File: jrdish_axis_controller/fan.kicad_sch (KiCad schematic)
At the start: 5 parts, among them CN5 KF2EDGR-2.54-2P, Q2 AO3400A

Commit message: PCB layout in progress
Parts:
- added C44: 10nF, PCM_JLCPCB:C_0402, symbol PCM_JLCPCB-Capacitors:0402,10nF
- added C45: 100nF, PCM_JLCPCB:C_0402, symbol PCM_JLCPCB-Capacitors:0402,100nF,(2)
- renumbered CN5 to CN6, R25 to R26, R26 to R27
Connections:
- net 12V: now also C44.1, C45.1
- net GND: now also C44.2, C45.2
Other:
- note added: "Place caps close to connector"
- company: (none) -> JRSeti
- moved on the sheet: CN6

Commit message: Continuing layout
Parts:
- renumbered C44 to C55, C45 to C56, CN6 to CN12, R26 to R27, R27 to R28
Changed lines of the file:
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@@
 		(in_pos_files yes)
 		(dnp no)
-		(property "Reference" "CN6"
+		(property "Reference" "CN12"
 			(at 117.348 76.454 0)
 			(show_name no)
@@
 			(project "jrdish_axis_controller"
 				(path "/10d7c3e5-be4d-4306-a59e-500b86bd141f/6fa2ea64-bed8-4819-9f4d-803f6e804a23"
-					(reference "CN6")
+					(reference "CN12")
 					(unit 1)
 				)
@@
 		(in_pos_files yes)
 		(dnp no)
-		(property "Reference" "#PWR040"
+		(property "Reference" "#PWR046"
 			(at 128.27 90.17 0)
 			(hide yes)
@@
 			(project "jrdish_axis_controller"
 				(path "/10d7c3e5-be4d-4306-a59e-500b86bd141f/6fa2ea64-bed8-4819-9f4d-803f6e804a23"
-					(reference "#PWR040")
+					(reference "#PWR046")
 					(unit 1)
 				)
@@
 		(dnp no)
 		(fields_autoplaced yes)
-		(property "Reference" "R26"
+		(property "Reference" "R27"
 			(at 133.35 90.17 90)
 			(show_name no)
@@
 			(project "jrdish_axis_controller"
 				(path "/10d7c3e5-be4d-4306-a59e-500b86bd141f/6fa2ea64-bed8-4819-9f4d-803f6e804a23"
-					(reference "R26")
+					(reference "R27")
 					(unit 1)
 				)
@@
 		(dnp no)
 		(fields_autoplaced yes)
-		(property "Reference" "R27"
+		(property "Reference" "R28"
 			(at 130.81 99.0599 0)
 			(show_name no)
@@
 			(project "jrdish_axis_controller"
 				(path "/10d7c3e5-be4d-4306-a59e-500b86bd141f/6fa2ea64-bed8-4819-9f4d-803f6e804a23"
-					(reference "R27")
+					(reference "R28")
 					(unit 1)
 				)
@@
 		(in_pos_files yes)
 		(dnp no)
-		(property "Reference" "C44"
+		(property "Reference" "C55"
 			(at 126.238 76.4539 0)
 			(show_name no)
@@
 			(project "jrdish_axis_controller"
 				(path "/10d7c3e5-be4d-4306-a59e-500b86bd141f/6fa2ea64-bed8-4819-9f4d-803f6e804a23"
-					(reference "C44")
+					(reference "C55")
 					(unit 1)
 				)
@@
 		(in_pos_files yes)
 		(dnp no)
-		(property "Reference" "#PWR041"
+		(property "Reference" "#PWR047"
 			(at 137.16 111.76 0)
 			(hide yes)
@@
 			(project "jrdish_axis_controller"
 				(path "/10d7c3e5-be4d-4306-a59e-500b86bd141f/6fa2ea64-bed8-4819-9f4d-803f6e804a23"
-					(reference "#PWR041")
+					(reference "#PWR047")
 					(unit 1)
 				)
@@
 		(in_pos_files yes)
 		(dnp no)
-		(property "Reference" "C45"
+		(property "Reference" "C56"
 			(at 133.604 76.1999 0)
 			(show_name no)
@@
 			(project "jrdish_axis_controller"
 				(path "/10d7c3e5-be4d-4306-a59e-500b86bd141f/6fa2ea64-bed8-4819-9f4d-803f6e804a23"
-					(reference "C45")
+					(reference "C56")
 					(unit 1)
 				)

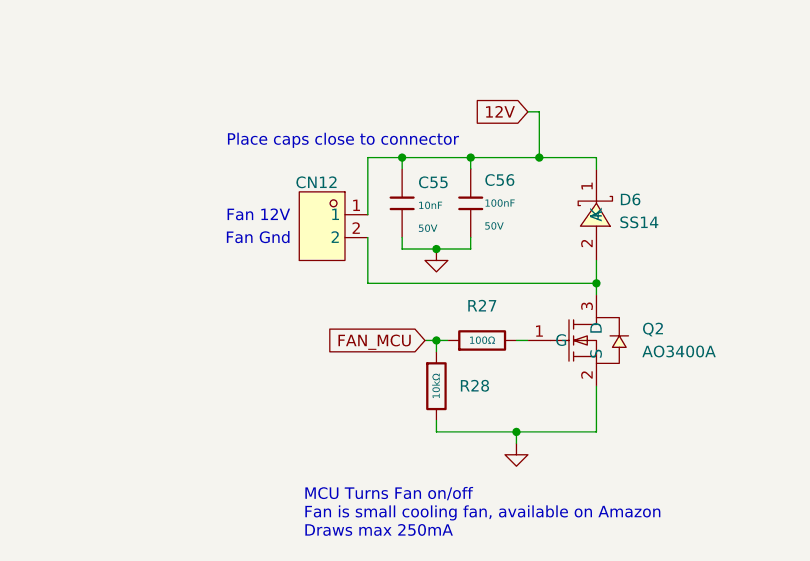
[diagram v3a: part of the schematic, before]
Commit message: RS485 isolated areas in place
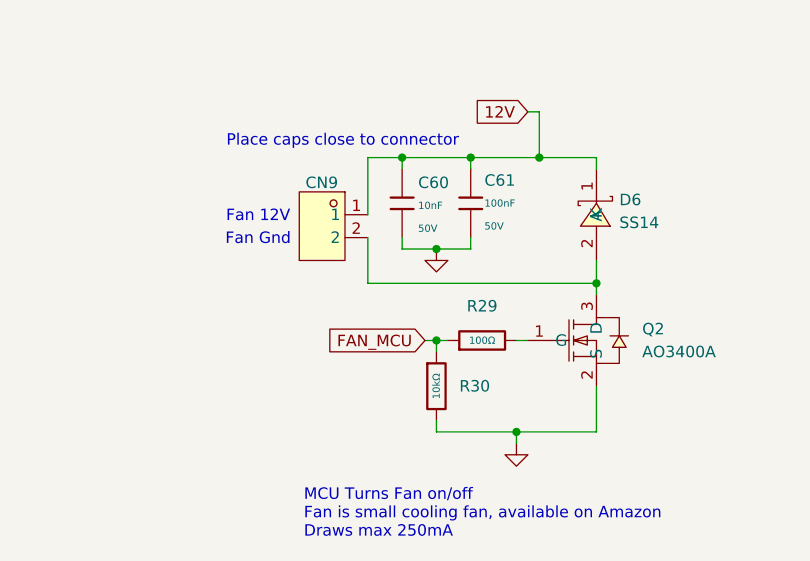
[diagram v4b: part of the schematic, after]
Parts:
- renumbered C55 to C60, C56 to C61, CN12 to CN9, R27 to R29, R28 to R30
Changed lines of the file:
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@@
 		(in_pos_files yes)
 		(dnp no)
-		(property "Reference" "CN12"
+		(property "Reference" "CN9"
 			(at 117.348 76.454 0)
 			(show_name no)
@@
 			(project "jrdish_axis_controller"
 				(path "/10d7c3e5-be4d-4306-a59e-500b86bd141f/6fa2ea64-bed8-4819-9f4d-803f6e804a23"
-					(reference "CN12")
+					(reference "CN9")
 					(unit 1)
 				)
@@
 		(dnp no)
 		(fields_autoplaced yes)
-		(property "Reference" "R27"
+		(property "Reference" "R29"
 			(at 133.35 90.17 90)
 			(show_name no)
@@
 			(project "jrdish_axis_controller"
 				(path "/10d7c3e5-be4d-4306-a59e-500b86bd141f/6fa2ea64-bed8-4819-9f4d-803f6e804a23"
-					(reference "R27")
+					(reference "R29")
 					(unit 1)
 				)
@@
 		(dnp no)
 		(fields_autoplaced yes)
-		(property "Reference" "R28"
+		(property "Reference" "R30"
 			(at 130.81 99.0599 0)
 			(show_name no)
@@
 			(project "jrdish_axis_controller"
 				(path "/10d7c3e5-be4d-4306-a59e-500b86bd141f/6fa2ea64-bed8-4819-9f4d-803f6e804a23"
-					(reference "R28")
+					(reference "R30")
 					(unit 1)
 				)
@@
 		(in_pos_files yes)
 		(dnp no)
-		(property "Reference" "C55"
+		(property "Reference" "C60"
 			(at 126.238 76.4539 0)
 			(show_name no)
@@
 			(project "jrdish_axis_controller"
 				(path "/10d7c3e5-be4d-4306-a59e-500b86bd141f/6fa2ea64-bed8-4819-9f4d-803f6e804a23"
-					(reference "C55")
+					(reference "C60")
 					(unit 1)
 				)
@@
 		(in_pos_files yes)
 		(dnp no)
-		(property "Reference" "C56"
+		(property "Reference" "C61"
 			(at 133.604 76.1999 0)
 			(show_name no)
@@
 			(project "jrdish_axis_controller"
 				(path "/10d7c3e5-be4d-4306-a59e-500b86bd141f/6fa2ea64-bed8-4819-9f4d-803f6e804a23"
-					(reference "C56")
+					(reference "C61")
 					(unit 1)
 				)

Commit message: Making refinements
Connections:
- net GND: no longer names the net of Q2.2 (S), R30.2
- net GND: no longer C60.2, C61.2
- new net: C60.2, C61.2
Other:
- title: (none) -> Fan
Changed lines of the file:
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@@
 	(paper "A4")
 	(title_block
-		(date "2026-04-12")
+		(title "Fan")
+		(date "2026-04-30")
 		(rev "1.0")
 		(company "JRSeti")

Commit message: Limit switches with mosfets
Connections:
- net GND: now reaches Q2.2 (S), R30.2
- net GND: now also C60.2, C61.2
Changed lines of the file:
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@@
 			)
 		)
-		(property "Datasheet" "https://lcsc.com/product-detail/MOSFET_AOS_AO3400A_AO3400A_C20917.html"
+		(property "Datasheet" "https://www.lcsc.com/datasheet/C15155.pdf?spm=wm.sxq.inf.ggs&lcsc_vid=FFBaV1wHQFldUVICFgBfBVJTQVJWXgBfEQRYBAFQE1YxVlNRQFdaUl1WQVlZUjtW"
 			(at 143.51 109.22 0)
 			(hide yes)

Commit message: Refinements...
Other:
- note added: "MCU Turns Fan on/off Fan is small DC cooling fan, available on Amazon Draws max 250mA"
- note removed: "MCU Turns Fan on/off Fan is small cooling fan, available on Amazon Draws max 250mA"
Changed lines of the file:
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@@
 		)
 	)
-	(text "MCU Turns Fan on/off\nFan is small cooling fan, available on Amazon\nDraws max 250mA"
+	(text "MCU Turns Fan on/off\nFan is small DC cooling fan, available on Amazon\nDraws max 250mA"
 		(exclude_from_sim no)
 		(at 113.538 113.284 0)
